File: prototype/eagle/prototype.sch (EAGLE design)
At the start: 43 parts, among them T1 3904, U1 ARDUINO_MINI_PRO, U2 ATA6663, U3 7805T, U4 FTDI-BOARD

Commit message: Renamed eagle prototype files.
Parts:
- S2: device my_lib:PUSH_BUTTON -> prototype:PUSH_BUTTON
- U1: device my_lib:ARDUINO_MINI_PRODIP24-6 -> prototype:ARDUINO_MINI_PRODIP24-6
- U2: device my_lib:ATA6663 -> prototype:ATA6663
- U4: device my_lib:FTDI-OBARD -> prototype:FTDI-OBARD
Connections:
- net N$15: now also U1.RESET; no longer U1.RST
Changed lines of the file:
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@@
 <part name="D4" library="display-hp" deviceset="HLMP6" device="" value="Green"/>
 <part name="D5" library="display-hp" deviceset="HLMP6" device="" value="Green"/>
-<part name="S2" library="my_lib" deviceset="PUSH_BUTTON" device=""/>
-<part name="U2" library="my_lib" deviceset="ATA6663" device=""/>
+<part name="S2" library="prototype" deviceset="PUSH_BUTTON" device=""/>
+<part name="U2" library="prototype" deviceset="ATA6663" device=""/>
 <part name="C1" library="rcl" deviceset="C-US" device="C0805" value="0.1uF"/>
 <part name="C2" library="rcl" deviceset="CPOL-US" device="SMCC" value="22uF"/>
 <part name="C3" library="rcl" deviceset="C-US" device="C0805" value="220pF"/>
 <part name="JP1" library="pinhead" deviceset="PINHD-1X3" device=""/>
-<part name="U4" library="my_lib" deviceset="FTDI-OBARD" device="" value="FTDI-BOARD"/>
+<part name="U4" library="prototype" deviceset="FTDI-OBARD" device="" value="FTDI-BOARD"/>
 <part name="U3" library="linear" deviceset="78*" device="T" technology="05"/>
 <part name="D8" library="diode" deviceset="MBRS3*0T3" device="" technology="2" value="1N5819"/>
 <part name="FRAME2" library="frames" deviceset="LETTER_L" device=""/>
 <part name="D6" library="diode" deviceset="MBRS3*0T3" device="" technology="2" value="1N5819"/>
-<part name="GND1" library="my_lib" deviceset="GND" device=""/>
-<part name="GND4" library="my_lib" deviceset="GND" device=""/>
-<part name="GND3" library="my_lib" deviceset="GND" device=""/>
-<part name="GND5" library="my_lib" deviceset="GND" device=""/>
-<part name="GND6" library="my_lib" deviceset="GND" device=""/>
-<part name="GND7" library="my_lib" deviceset="GND" device=""/>
-<part name="GND8" library="my_lib" deviceset="GND" device=""/>
-<part name="GND9" library="my_lib" deviceset="GND" device=""/>
-<part name="GND10" library="my_lib" deviceset="GND" device=""/>
-<part name="GND11" library="my_lib" deviceset="GND" device=""/>
+<part name="GND1" library="prototype" deviceset="GND" device=""/>
+<part name="GND4" library="prototype" deviceset="GND" device=""/>
+<part name="GND3" library="prototype" deviceset="GND" device=""/>
+<part name="GND5" library="prototype" deviceset="GND" device=""/>
+<part name="GND6" library="prototype" deviceset="GND" device=""/>
+<part name="GND7" library="prototype" deviceset="GND" device=""/>
+<part name="GND8" library="prototype" deviceset="GND" device=""/>
+<part name="GND9" library="prototype" deviceset="GND" device=""/>
+<part name="GND10" library="prototype" deviceset="GND" device=""/>
+<part name="GND11" library="prototype" deviceset="GND" device=""/>
 <part name="C4" library="rcl" deviceset="C-US" device="C0805" value="0.1uF"/>
-<part name="GND12" library="my_lib" deviceset="GND" device=""/>
-<part name="U1" library="my_lib" deviceset="ARDUINO_MINI_PRO" device="DIP24-6" value="ARDUINO_MINI_PRO"/>
+<part name="GND12" library="prototype" deviceset="GND" device=""/>
+<part name="U1" library="prototype" deviceset="ARDUINO_MINI_PRO" device="DIP24-6" value="ARDUINO_MINI_PRO"/>
 <part name="C6" library="rcl" deviceset="C-US" device="C0805" value="10nF"/>
 <part name="P+2" library="supply1" deviceset="+5V" device=""/>
@@
 <part name="R9" library="rcl" deviceset="R-US_" device="R0805" value="5K"/>
 <part name="P+1" library="supply1" deviceset="+5V" device=""/>
-<part name="GND2" library="my_lib" deviceset="GND" device=""/>
-<part name="GND13" library="my_lib" deviceset="GND" device=""/>
-<part name="GND15" library="my_lib" deviceset="GND" device=""/>
+<part name="GND2" library="prototype" deviceset="GND" device=""/>
+<part name="GND13" library="prototype" deviceset="GND" device=""/>
+<part name="GND15" library="prototype" deviceset="GND" device=""/>
 <part name="P+4" library="supply1" deviceset="+5V" device=""/>
 <part name="BREAK" library="testpad" deviceset="TP" device="PAD1-17"/>
 <part name="SAMPLE" library="testpad" deviceset="TP" device="PAD1-17"/>
 <part name="ERROR" library="testpad" deviceset="TP" device="PAD1-17"/>
-<part name="GND16" library="my_lib" deviceset="GND" device=""/>
+<part name="GND16" library="prototype" deviceset="GND" device=""/>
 <part name="F2" library="special" deviceset="FUSE" device="" value="200ma"/>
 <part name="JP2" library="pinhead" deviceset="PINHD-2X3" device="" value="ICSP"/>
-<part name="GND14" library="my_lib" deviceset="GND" device=""/>
+<part name="GND14" library="prototype" deviceset="GND" device=""/>
 <part name="P+5" library="supply1" deviceset="+5V" device=""/>
 <part name="DEBUG1" library="testpad" deviceset="TP" device="PAD1-17"/>
 <part name="DEBUG2" library="testpad" deviceset="TP" device="PAD1-17"/>
 <part name="S1" library="switch-dil" deviceset="DS01E" device=""/>
-<part name="GND17" library="my_lib" deviceset="GND" device=""/>
+<part name="GND17" library="prototype" deviceset="GND" device=""/>
 <part name="ISR" library="testpad" deviceset="TP" device="PAD1-17"/>
 <part name="SG1" library="buzzer" deviceset="F/SMX" device="" value=""/>
 <part name="R1" library="rcl" deviceset="R-US_" device="R0805" value="5K"/>
 <part name="T1" library="transistor" deviceset="*-NPN-" device="SOT23-BEC" technology="MMBT3904LT1" value="3904"/>
-<part name="GND18" library="my_lib" deviceset="GND" device=""/>
+<part name="GND18" library="prototype" deviceset="GND" device=""/>
 <part name="D1" library="diode" deviceset="DIODE-" device="MINIMELF"/>
 <part name="P+3" library="supply1" deviceset="+5V" device=""/>
@@
 <wire x1="165.1" y1="96.52" x2="165.1" y2="101.6" width="0.1524" layer="91"/>
 <pinref part="C6" gate="G$1" pin="2"/>
-<pinref part="U1" gate="G$1" pin="RST"/>
+<pinref part="U1" gate="G$1" pin="RESET"/>
 <wire x1="180.34" y1="101.6" x2="175.26" y2="101.6" width="0.1524" layer="91"/>
 <wire x1="175.26" y1="101.6" x2="175.26" y2="71.12" width="0.1524" layer="91"/>

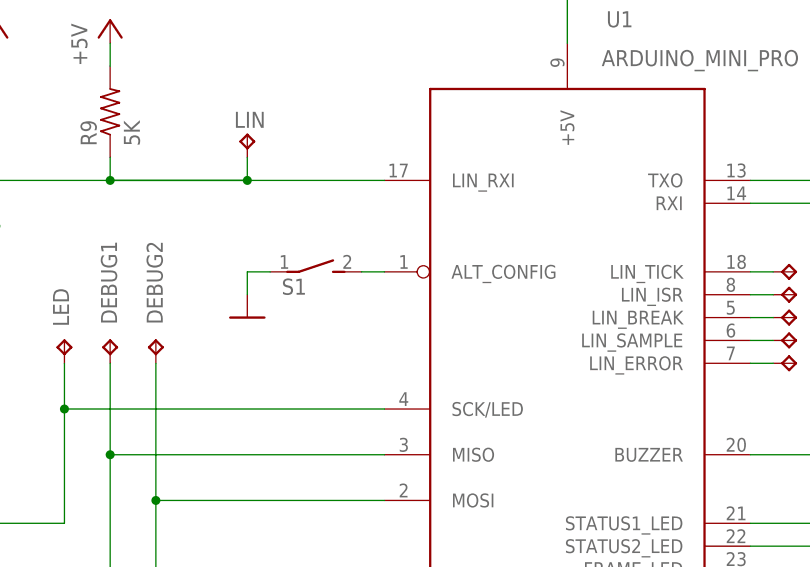
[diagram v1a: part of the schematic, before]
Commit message: Simplify the config and the communication with the ISR.
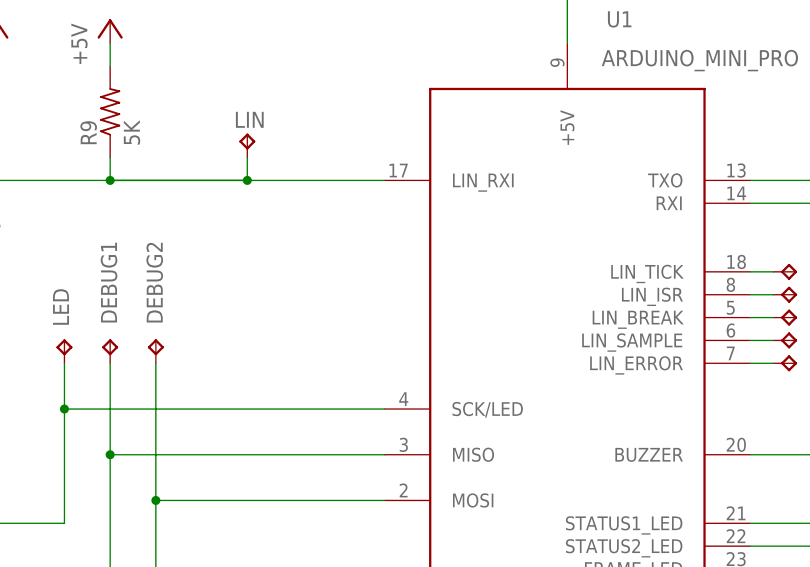
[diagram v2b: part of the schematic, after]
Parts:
- removed S1: (no value), switch-dil:DS01E
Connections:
- removed net N$27: S1.2, U1.ALT_CONFIG
- net GND: no longer S1.1
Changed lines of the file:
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@@
 <part name="DEBUG1" library="testpad" deviceset="TP" device="PAD1-17"/>
 <part name="DEBUG2" library="testpad" deviceset="TP" device="PAD1-17"/>
-<part name="S1" library="switch-dil" deviceset="DS01E" device=""/>
-<part name="GND17" library="prototype" deviceset="GND" device=""/>
 <part name="ISR" library="testpad" deviceset="TP" device="PAD1-17"/>
 <part name="SG1" library="buzzer" deviceset="F/SMX" device="" value=""/>
@@
 <attribute name="TP_SIGNAL_NAME" x="156.21" y="128.27" size="1.778" layer="97"/>
 </instance>
-<instance part="S1" gate="1" x="172.72" y="137.16" rot="R270"/>
-<instance part="GND17" gate="1" x="165.1" y="132.08"/>
 <instance part="ISR" gate="G$1" x="226.06" y="134.62" smashed="yes" rot="R270">
 <attribute name="NAME" x="227.838" y="133.858" size="1.778" layer="95"/>
@@
 <wire x1="121.92" y1="83.82" x2="129.54" y2="83.82" width="0.1524" layer="91"/>
 <wire x1="129.54" y1="83.82" x2="129.54" y2="78.74" width="0.1524" layer="91"/>
-</segment>
-<segment>
-<pinref part="S1" gate="1" pin="1"/>
-<pinref part="GND17" gate="1" pin="GND"/>
-<wire x1="167.64" y1="137.16" x2="165.1" y2="137.16" width="0.1524" layer="91"/>
-<wire x1="165.1" y1="137.16" x2="165.1" y2="134.62" width="0.1524" layer="91"/>
 </segment>
 <segment>
@@
 </segment>
 </net>
-<net name="N$27" class="0">
-<segment>
-<pinref part="S1" gate="1" pin="2"/>
-<pinref part="U1" gate="G$1" pin="ALT_CONFIG"/>
-<wire x1="177.8" y1="137.16" x2="180.34" y2="137.16" width="0.1524" layer="91"/>
-</segment>
-</net>

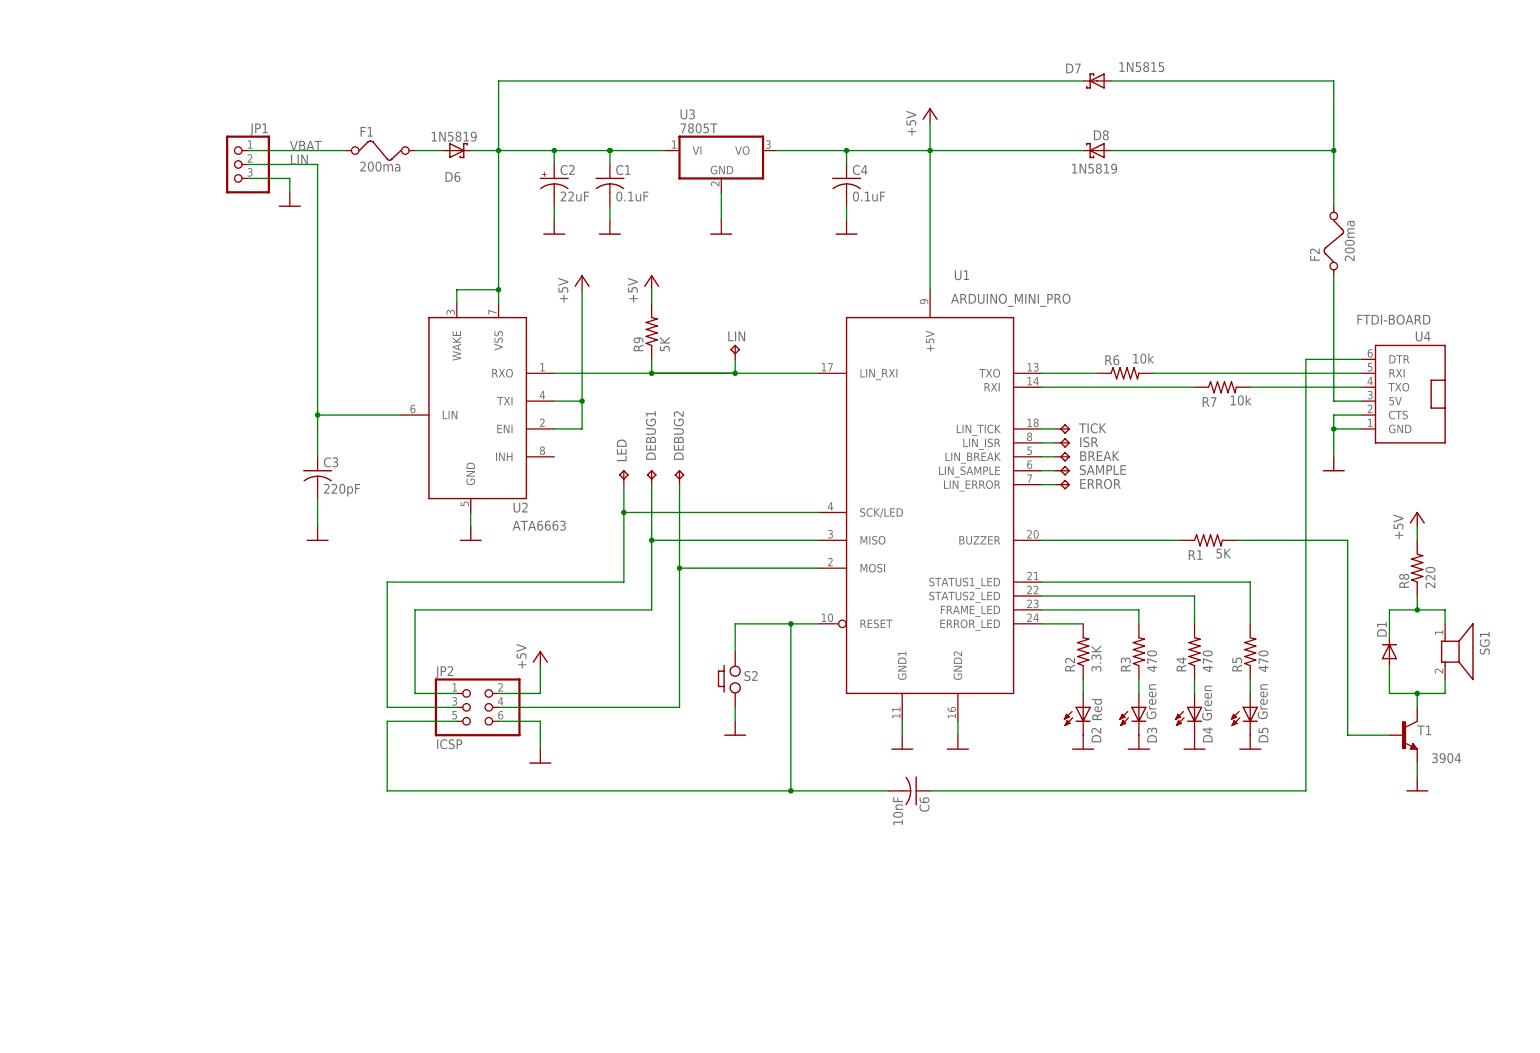
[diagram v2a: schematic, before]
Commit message: Changed the lin chip from ata6663 to ata6631 (built in LDO).
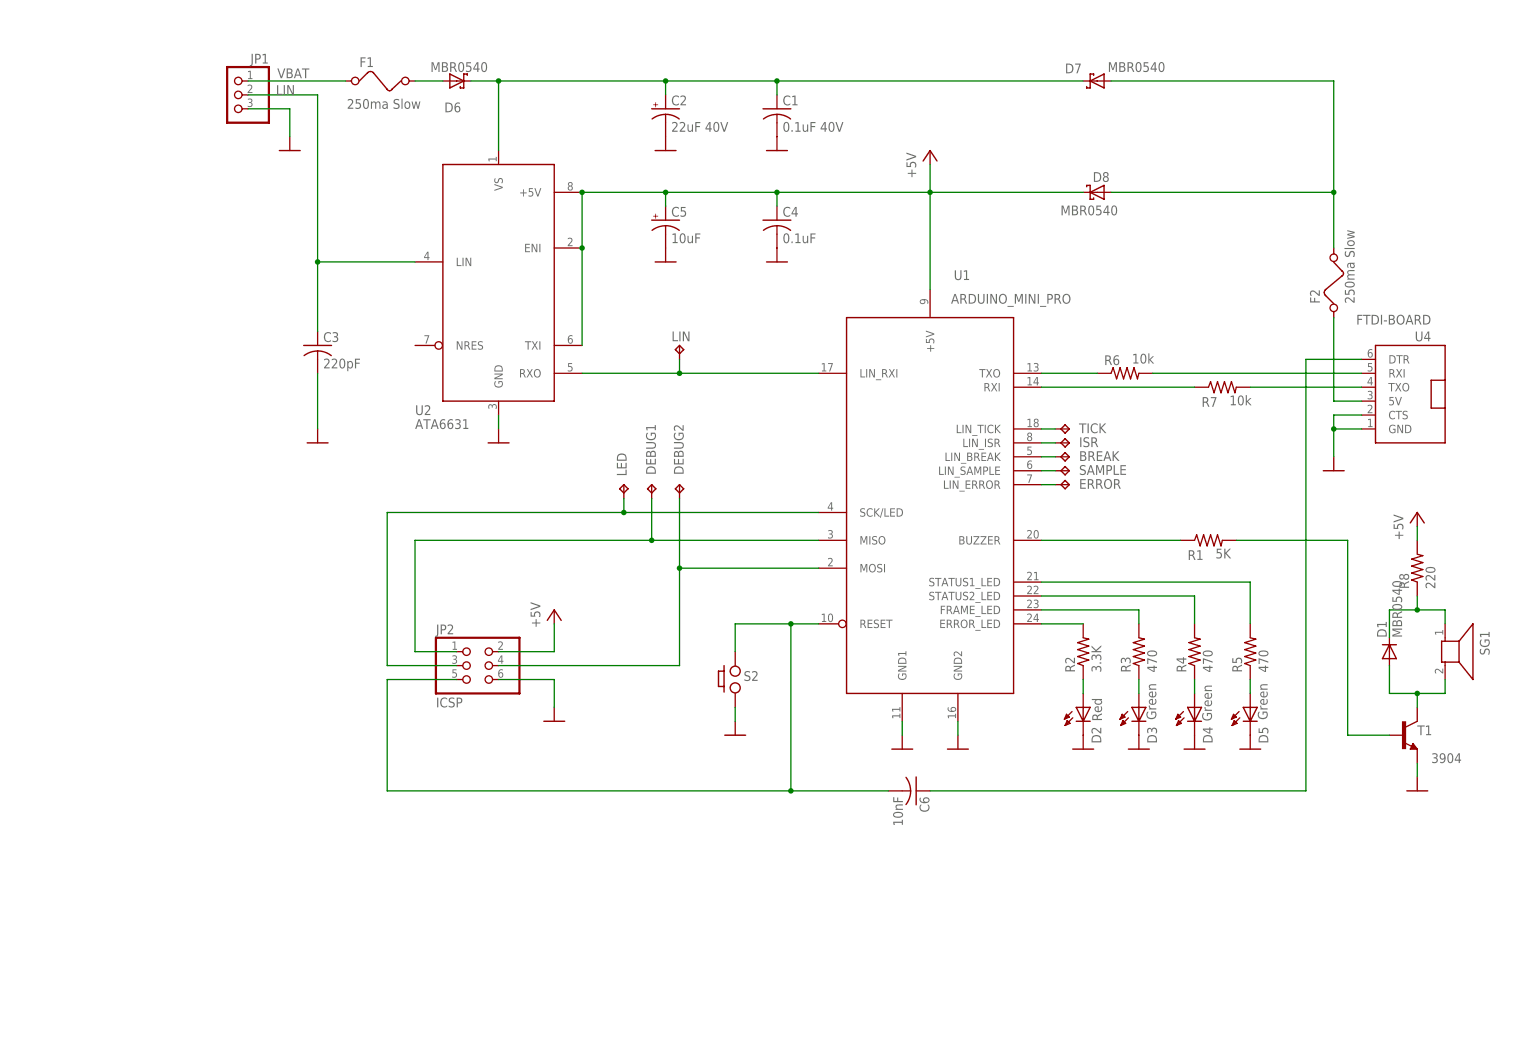
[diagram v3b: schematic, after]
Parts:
- removed R9: 5K, rcl:R-US_R0805
- removed U3: 7805T, linear:7805T
- added C5: 10uF, rcl:CPOL-USSMCC
- C1: value 0.1uF -> 0.1uF 40V
- C2: value 22uF -> 22uF 40V
- D1: value (none) -> MBR0540
- D6, D8: value 1N5819 -> MBR0540
- D7: value 1N5815 -> MBR0540
- F1, F2: value 200ma -> 250ma Slow
- U2: value ATA6663 -> ATA6631; device prototype:ATA6663 -> beeper:ATA6631
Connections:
- net +12V: now also U2.VS; no longer U2.VSS, U2.WAKE, U3.VI
- net +5V: now also C5.+, U2.+5V; no longer R9.2, U3.VO
- net GND: now also C5.-; no longer U3.GND
- net N$18: no longer R9.1
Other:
- moved on the sheet: C1, C2, C3, C4, D6, D8, DEBUG1, DEBUG2, F1, F2, JP1, JP2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
